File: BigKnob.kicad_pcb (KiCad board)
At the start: 2 copper layers, 45 x 80 mm, 11 parts, among them J1 NSJ12HF-1, J2 NSJ12HF-1, J3 NSJ12HF-1, J4 STEREO-JACK-SWITCHED-5-Pin, J5 STEREO-JACK-SWITCHED-5-Pin

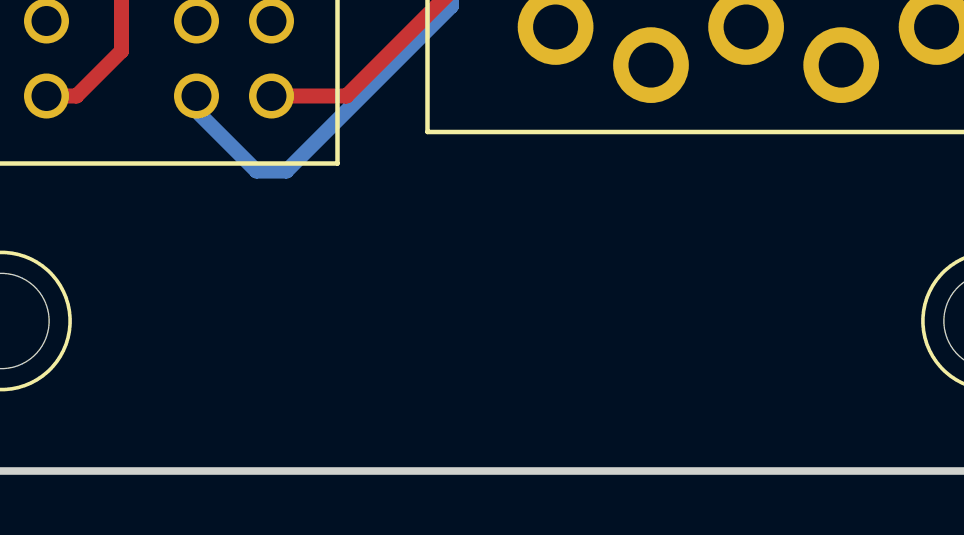
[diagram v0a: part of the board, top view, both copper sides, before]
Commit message: add oshw logo :cake:
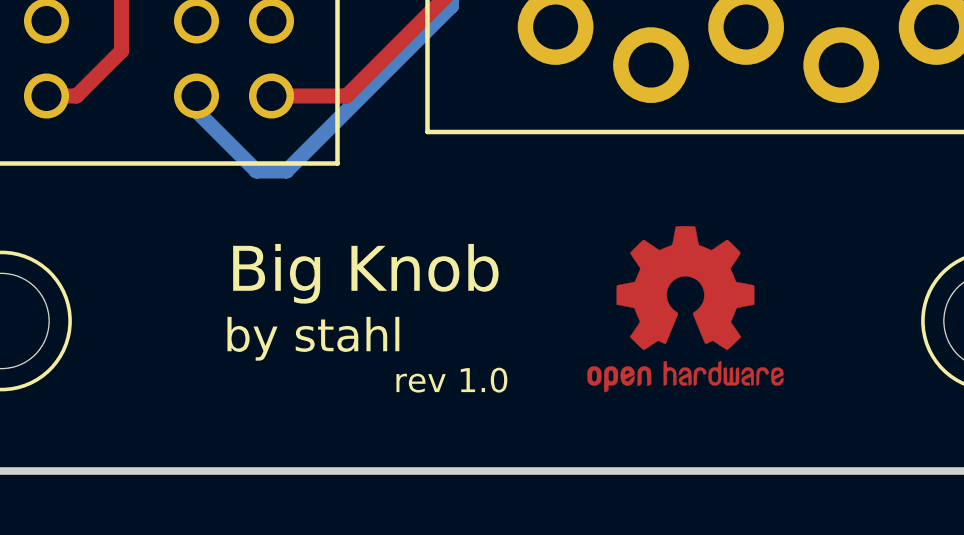
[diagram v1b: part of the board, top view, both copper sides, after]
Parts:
- added REF***: OSHW-Logo2_7.3x6mm_Copper, Symbols:OSHW-Logo2_7.3x6mm_Copper, F.Cu at (157.2, 122.2)
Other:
- board text added: "Big Knob"
- board text added: "by stahl"
- board text added: "rev 1.0"

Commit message: :punch: fixed schema
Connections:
- R1 pad A2: CHASSIS_GND -> Net-(J3-Pad5)
- R1 pad A3: Net-(J3-Pad5) -> CHASSIS_GND
- R1 pad B2: CHASSIS_GND -> Net-(J3-Pad3)
- R1 pad B3: Net-(J3-Pad3) -> CHASSIS_GND
- R1 pad C2: (no net) -> Net-(J3-Pad11)
- R1 pad C3: Net-(J3-Pad11) -> CHASSIS_GND
- R1 pad D2: CHASSIS_GND -> Net-(J3-Pad9)
- R1 pad D3: Net-(J3-Pad9) -> CHASSIS_GND
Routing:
- net Net-(J3-Pad11): track 25.6 -> 30.4 mm
- net Net-(J3-Pad5): track 33.8 -> 29.2 mm
- net Net-(J3-Pad3): track 33.2 -> 31.7 mm
- net Net-(J3-Pad9): track 24.7 -> 23.7 mm

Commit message: :punch: v1.1
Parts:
- moved S1 16.2 mm to (151.8, 91.0), turned to 180 degrees
- moved J1 11.1 mm to (173.4, 56.5)
- moved J4 11.0 mm to (130.3, 66.6)
- moved J5 11.0 mm to (130.3, 53.6)
- moved J2 10.8 mm to (173.4, 74.8)
- moved REF** 10.0 mm to (168.3, 42.6)
- moved REF** 10.0 mm to (135.3, 42.6)
- moved R1 4.47 mm to (130.3, 108.6)
- moved REF** 1.41 mm to (135.3, 121.6)
- moved REF** 1.41 mm to (168.3, 121.6)
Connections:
- R1 pad A1: Net-(R1-PadA1) -> CHASSIS_GND
- R1 pad A3: CHASSIS_GND -> Net-(R1-PadA3)
- R1 pad B1: Net-(R1-PadB1) -> CHASSIS_GND
- R1 pad B3: CHASSIS_GND -> Net-(R1-PadB3)
- R1 pad C1: Net-(R1-PadC1) -> CHASSIS_GND
- R1 pad C3: CHASSIS_GND -> Net-(R1-PadC3)
- R1 pad D1: Net-(R1-PadD1) -> CHASSIS_GND
- R1 pad D3: CHASSIS_GND -> Net-(R1-PadD3)
- S1 pad 11: Net-(R1-PadD1) -> Net-(R1-PadD3)
- S1 pad 2: Net-(R1-PadA1) -> Net-(R1-PadA3)
- S1 pad 5: Net-(R1-PadB1) -> Net-(R1-PadB3)
- S1 pad 8: Net-(R1-PadC1) -> Net-(R1-PadC3)
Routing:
- net Net-(R1-PadA3): track 0.00 -> 44.3 mm
- net Net-(R1-PadB3): track 0.00 -> 35.8 mm
- net Net-(R1-PadD1): track 34.1 -> 0.00 mm, vias 1 -> 0
- net Net-(J1-Pad11): track 56.8 -> 88.0 mm
- net CHASSIS_GND: track 0.00 -> 30.5 mm, vias 0 -> 1
- net Net-(R1-PadD3): track 0.00 -> 27.7 mm
- net Net-(R1-PadC3): track 0.00 -> 23.8 mm
- net Net-(R1-PadC1): track 19.4 -> 0.00 mm
- net Net-(R1-PadA1): track 18.9 -> 0.00 mm
- net Net-(J3-Pad11): track 30.4 -> 16.1 mm
- net Net-(R1-PadB1): track 13.8 -> 0.00 mm, vias 1 -> 0
- net Net-(J2-Pad9): track 25.4 -> 38.0 mm, vias 1 -> 0
- net Net-(J2-Pad3): track 27.6 -> 39.4 mm
- net Net-(J2-Pad5): track 47.9 -> 37.3 mm
- net Net-(J1-Pad9): track 46.9 -> 57.2 mm, vias 1 -> 2
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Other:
- board size 45 x 80 mm -> 43 x 89 mm
- board text added: "2 x unbalanced stereo mini-jack input 2 x balanced stereo input balanced stereo output volume pot"
- board text added: "passive audio switch"
- board text added: "rev 1.1"
- board text removed: "rev 1.0"
